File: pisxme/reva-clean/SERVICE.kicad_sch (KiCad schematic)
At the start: 5 parts

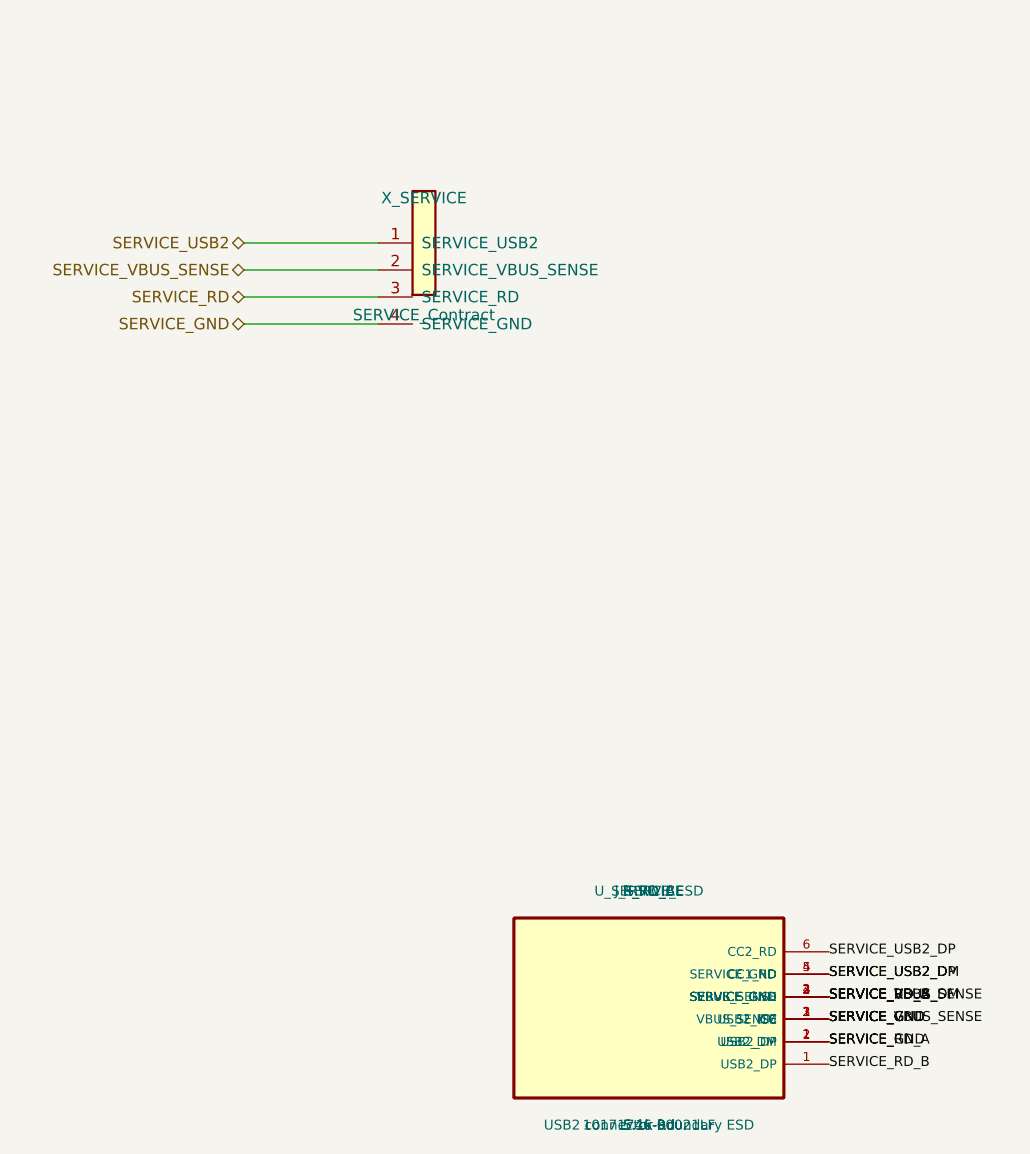
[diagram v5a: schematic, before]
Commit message: fix KiCad annotation and netlist export
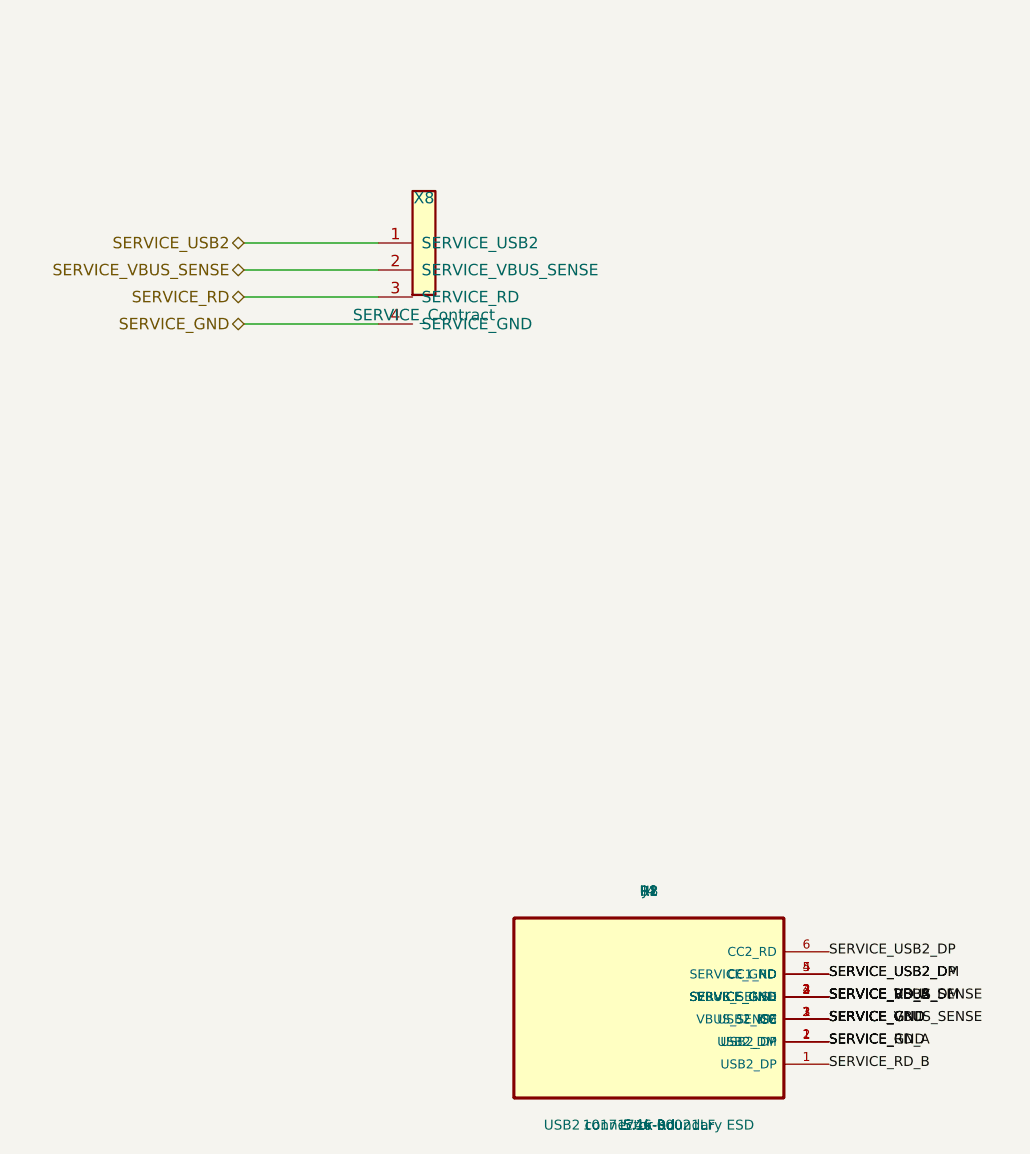
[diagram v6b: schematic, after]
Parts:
- R1: renamed from R_RD_A; footprint (none) -> PiSXMeRevAClean:USB_C_SERVICE_10171746
- U8: renamed from U_SERVICE_ESD; footprint PiSXMeRevAClean:USB_C_SERVICE_10171746 -> (none)
- renumbered J_SERVICE to J4, R_RD_B to R2, X_SERVICE to X8
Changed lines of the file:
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@@
     (on_board no)
     (dnp no)
-    (property "Reference" "X_SERVICE"
+    (property "Reference" "X8"
       (at 25 5 0)
       (effects (font (size 1.27 1.27))))
@@
     (pin "4")
     (instances (project "PiSXMe_RevA_Clean"
-      (path "/30000000-0000-0000-0000-000000000000/10000000-0000-0000-0000-000000000008" (reference "X_SERVICE" ) (unit 1))))
+      (path "/30000000-0000-0000-0000-000000000000/10000000-0000-0000-0000-000000000008" (reference "X8" ) (unit 1))))
   )
 (label "SERVICE_USB2_DP" (at 70 88.75 0) (effects (font (size 1.1 1.1)) (justify left)))
@@
 (label "SERVICE_RD_A" (at 70 98.75 0) (effects (font (size 1.1 1.1)) (justify left)))
 (label "SERVICE_RD_B" (at 70 101.25 0) (effects (font (size 1.1 1.1)) (justify left)))
-(symbol (lib_id "PiSXMeRevAClean:USB2_UFP_CONNECTOR") (at 50 95 0) (unit 1) (exclude_from_sim no) (in_bom yes) (on_board yes) (dnp no) (property "Reference" "J_SERVICE" (at 50 82 0) (effects (font (size 1.1 1.1)))) (property "Value" "10171746-00021LF" (at 50 108 0) (effects (font (size 1.1 1.1)))) (property "MPN" "10171746-00021LF" (at 50 95 0) (effects (font (size 1 1)) (hide yes))) (property "Footprint" "PiSXMeRevAClean:USB_C_SERVICE_10171746" (at 50 95 0) (effects (font (size 1 1)) (hide yes))) (pin "1")
+(symbol (lib_id "PiSXMeRevAClean:USB2_UFP_CONNECTOR") (at 50 95 0) (unit 1) (exclude_from_sim no) (in_bom yes) (on_board yes) (dnp no) (property "Reference" "J4" (at 50 82 0) (effects (font (size 1.1 1.1)))) (property "Value" "10171746-00021LF" (at 50 108 0) (effects (font (size 1.1 1.1)))) (property "MPN" "10171746-00021LF" (at 50 95 0) (effects (font (size 1 1)) (hide yes))) (property "Footprint" "PiSXMeRevAClean:USB_C_SERVICE_10171746" (at 50 95 0) (effects (font (size 1 1)) (hide yes))) (pin "1")
 (pin "2")
 (pin "3")
 (pin "4")
 (pin "5")
-(pin "6") (instances (project "PiSXMe_RevA_Clean" (path "/30000000-0000-0000-0000-000000000000" (reference "J_SERVICE") (unit 1)))) )(label "SERVICE_USB2_DP" (at 70 91.25 0) (effects (font (size 1.1 1.1)) (justify left)))
+(pin "6") (instances (project "PiSXMe_RevA_Clean" (path "/30000000-0000-0000-0000-000000000000" (reference "J4") (unit 1)))) )(label "SERVICE_USB2_DP" (at 70 91.25 0) (effects (font (size 1.1 1.1)) (justify left)))
 (label "SERVICE_USB2_DM" (at 70 93.75 0) (effects (font (size 1.1 1.1)) (justify left)))
 (label "SERVICE_VBUS_SENSE" (at 70 96.25 0) (effects (font (size 1.1 1.1)) (justify left)))
 (label "SERVICE_GND" (at 70 98.75 0) (effects (font (size 1.1 1.1)) (justify left)))
-(symbol (lib_id "PiSXMeRevAClean:USB2_ESD") (at 50 95 0) (unit 1) (exclude_from_sim no) (in_bom yes) (on_board yes) (dnp no) (property "Reference" "U_SERVICE_ESD" (at 50 82 0) (effects (font (size 1.1 1.1)))) (property "Value" "USB2 connector-boundary ESD" (at 50 108 0) (effects (font (size 1.1 1.1)))) (property "MPN" "USB2 connector-boundary ESD" (at 50 95 0) (effects (font (size 1 1)) (hide yes))) (property "Footprint" "PiSXMeRevAClean:USB_C_SERVICE_10171746" (at 50 95 0) (effects (font (size 1 1)) (hide yes))) (pin "1")
+(symbol (lib_id "PiSXMeRevAClean:USB2_ESD") (at 50 95 0) (unit 1) (exclude_from_sim no) (in_bom yes) (on_board yes) (dnp no) (property "Reference" "U8" (at 50 82 0) (effects (font (size 1.1 1.1)))) (property "Value" "USB2 connector-boundary ESD" (at 50 108 0) (effects (font (size 1.1 1.1)))) (property "MPN" "USB2 connector-boundary ESD" (at 50 95 0) (effects (font (size 1 1)) (hide yes))) (property "Footprint" "" (at 50 95 0) (effects (font (size 1 1)) (hide yes))) (pin "1")
 (pin "2")
 (pin "3")
-(pin "4") (instances (project "PiSXMe_RevA_Clean" (path "/30000000-0000-0000-0000-000000000000" (reference "U_SERVICE_ESD") (unit 1)))) )(label "SERVICE_RD_A" (at 70 93.75 0) (effects (font (size 1.1 1.1)) (justify left)))
+(pin "4") (instances (project "PiSXMe_RevA_Clean" (path "/30000000-0000-0000-0000-000000000000" (reference "U8") (unit 1)))) )(label "SERVICE_RD_A" (at 70 93.75 0) (effects (font (size 1.1 1.1)) (justify left)))
 (label "SERVICE_GND" (at 70 96.25 0) (effects (font (size 1.1 1.1)) (justify left)))
-(symbol (lib_id "PiSXMeRevAClean:USB2_RD_5K1") (at 50 95 0) (unit 1) (exclude_from_sim no) (in_bom yes) (on_board yes) (dnp no) (property "Reference" "R_RD_A" (at 50 82 0) (effects (font (size 1.1 1.1)))) (property "Value" "5.1k Rd" (at 50 108 0) (effects (font (size 1.1 1.1)))) (property "MPN" "5.1k Rd" (at 50 95 0) (effects (font (size 1 1)) (hide yes))) (property "Footprint" "" (at 50 95 0) (effects (font (size 1 1)) (hide yes))) (pin "1")
-(pin "2") (instances (project "PiSXMe_RevA_Clean" (path "/30000000-0000-0000-0000-000000000000" (reference "R_RD_A") (unit 1)))) )(label "SERVICE_RD_B" (at 70 93.75 0) (effects (font (size 1.1 1.1)) (justify left)))
+(symbol (lib_id "PiSXMeRevAClean:USB2_RD_5K1") (at 50 95 0) (unit 1) (exclude_from_sim no) (in_bom yes) (on_board yes) (dnp no) (property "Reference" "R1" (at 50 82 0) (effects (font (size 1.1 1.1)))) (property "Value" "5.1k Rd" (at 50 108 0) (effects (font (size 1.1 1.1)))) (property "MPN" "5.1k Rd" (at 50 95 0) (effects (font (size 1 1)) (hide yes))) (property "Footprint" "PiSXMeRevAClean:USB_C_SERVICE_10171746" (at 50 95 0) (effects (font (size 1 1)) (hide yes))) (pin "1")
+(pin "2") (instances (project "PiSXMe_RevA_Clean" (path "/30000000-0000-0000-0000-000000000000" (reference "R1") (unit 1)))) )(label "SERVICE_RD_B" (at 70 93.75 0) (effects (font (size 1.1 1.1)) (justify left)))
 (label "SERVICE_GND" (at 70 96.25 0) (effects (font (size 1.1 1.1)) (justify left)))
-(symbol (lib_id "PiSXMeRevAClean:USB2_RD_5K1") (at 50 95 0) (unit 1) (exclude_from_sim no) (in_bom yes) (on_board yes) (dnp no) (property "Reference" "R_RD_B" (at 50 82 0) (effects (font (size 1.1 1.1)))) (property "Value" "5.1k Rd" (at 50 108 0) (effects (font (size 1.1 1.1)))) (property "MPN" "5.1k Rd" (at 50 95 0) (effects (font (size 1 1)) (hide yes))) (property "Footprint" "" (at 50 95 0) (effects (font (size 1 1)) (hide yes))) (pin "1")
-(pin "2") (instances (project "PiSXMe_RevA_Clean" (path "/30000000-0000-0000-0000-000000000000" (reference "R_RD_B") (unit 1)))) )
+(symbol (lib_id "PiSXMeRevAClean:USB2_RD_5K1") (at 50 95 0) (unit 1) (exclude_from_sim no) (in_bom yes) (on_board yes) (dnp no) (property "Reference" "R2" (at 50 82 0) (effects (font (size 1.1 1.1)))) (property "Value" "5.1k Rd" (at 50 108 0) (effects (font (size 1.1 1.1)))) (property "MPN" "5.1k Rd" (at 50 95 0) (effects (font (size 1 1)) (hide yes))) (property "Footprint" "" (at 50 95 0) (effects (font (size 1 1)) (hide yes))) (pin "1")
+(pin "2") (instances (project "PiSXMe_RevA_Clean" (path "/30000000-0000-0000-0000-000000000000" (reference "R2") (unit 1)))) )
   (sheet_instances (path "/30000000-0000-0000-0000-000000000000/10000000-0000-0000-0000-000000000008" (page "8")))
 )

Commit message: close service ESD electrical authority
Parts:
- U8: value USB2 connector-boundary ESD -> TPD2EUSB30DRTR; footprint (none) -> PiSXMeRevAClean:USB_C_SERVICE_10171746; MPN USB2 connector-boundary ESD -> TPD2EUSB30DRTR
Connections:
- net SERVICE_GND: no longer U8.4 (SERVICE_GND)
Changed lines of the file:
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@@
 (label "SERVICE_VBUS_SENSE" (at 70 96.25 0) (effects (font (size 1.1 1.1)) (justify left)))
 (label "SERVICE_GND" (at 70 98.75 0) (effects (font (size 1.1 1.1)) (justify left)))
-(symbol (lib_id "PiSXMeRevAClean:USB2_ESD") (at 50 95 0) (unit 1) (exclude_from_sim no) (in_bom yes) (on_board yes) (dnp no) (property "Reference" "U8" (at 50 82 0) (effects (font (size 1.1 1.1)))) (property "Value" "USB2 connector-boundary ESD" (at 50 108 0) (effects (font (size 1.1 1.1)))) (property "MPN" "USB2 connector-boundary ESD" (at 50 95 0) (effects (font (size 1 1)) (hide yes))) (property "Footprint" "" (at 50 95 0) (effects (font (size 1 1)) (hide yes))) (pin "1")
+(label "SERVICE_USB2_DP" (at 70 92.5 0) (effects (font (size 1.1 1.1)) (justify left)))
+(label "SERVICE_USB2_DM" (at 70 95 0) (effects (font (size 1.1 1.1)) (justify left)))
+(label "SERVICE_GND" (at 70 97.5 0) (effects (font (size 1.1 1.1)) (justify left)))
+(symbol (lib_id "PiSXMeRevAClean:USB2_ESD") (at 50 95 0) (unit 1) (exclude_from_sim no) (in_bom yes) (on_board yes) (dnp no) (property "Reference" "U8" (at 50 82 0) (effects (font (size 1.1 1.1)))) (property "Value" "TPD2EUSB30DRTR" (at 50 108 0) (effects (font (size 1.1 1.1)))) (property "MPN" "TPD2EUSB30DRTR" (at 50 95 0) (effects (font (size 1 1)) (hide yes))) (property "Footprint" "PiSXMeRevAClean:USB_C_SERVICE_10171746" (at 50 95 0) (effects (font (size 1 1)) (hide yes))) (pin "1")
 (pin "2")
-(pin "3")
-(pin "4") (instances (project "PiSXMe_RevA_Clean" (path "/30000000-0000-0000-0000-000000000000" (reference "U8") (unit 1)))) )(label "SERVICE_RD_A" (at 70 93.75 0) (effects (font (size 1.1 1.1)) (justify left)))
+(pin "3") (instances (project "PiSXMe_RevA_Clean" (path "/30000000-0000-0000-0000-000000000000" (reference "U8") (unit 1)))) )(label "SERVICE_RD_A" (at 70 93.75 0) (effects (font (size 1.1 1.1)) (justify left)))
 (label "SERVICE_GND" (at 70 96.25 0) (effects (font (size 1.1 1.1)) (justify left)))
 (symbol (lib_id "PiSXMeRevAClean:USB2_RD_5K1") (at 50 95 0) (unit 1) (exclude_from_sim no) (in_bom yes) (on_board yes) (dnp no) (property "Reference" "R1" (at 50 82 0) (effects (font (size 1.1 1.1)))) (property "Value" "5.1k Rd" (at 50 108 0) (effects (font (size 1.1 1.1)))) (property "MPN" "5.1k Rd" (at 50 95 0) (effects (font (size 1 1)) (hide yes))) (property "Footprint" "PiSXMeRevAClean:USB_C_SERVICE_10171746" (at 50 95 0) (effects (font (size 1 1)) (hide yes))) (pin "1")

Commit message: close service ESD footprint authority
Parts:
- R1: footprint PiSXMeRevAClean:USB_C_SERVICE_10171746 -> PiSXMeRevAClean:R_0402_1005Metric
- R2: footprint (none) -> PiSXMeRevAClean:R_0402_1005Metric
- U8: footprint PiSXMeRevAClean:USB_C_SERVICE_10171746 -> PiSXMeRevAClean:Texas_DRT_3
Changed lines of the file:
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@@
 (label "SERVICE_USB2_DM" (at 70 95 0) (effects (font (size 1.1 1.1)) (justify left)))
 (label "SERVICE_GND" (at 70 97.5 0) (effects (font (size 1.1 1.1)) (justify left)))
-(symbol (lib_id "PiSXMeRevAClean:USB2_ESD") (at 50 95 0) (unit 1) (exclude_from_sim no) (in_bom yes) (on_board yes) (dnp no) (property "Reference" "U8" (at 50 82 0) (effects (font (size 1.1 1.1)))) (property "Value" "TPD2EUSB30DRTR" (at 50 108 0) (effects (font (size 1.1 1.1)))) (property "MPN" "TPD2EUSB30DRTR" (at 50 95 0) (effects (font (size 1 1)) (hide yes))) (property "Footprint" "PiSXMeRevAClean:USB_C_SERVICE_10171746" (at 50 95 0) (effects (font (size 1 1)) (hide yes))) (pin "1")
+(symbol (lib_id "PiSXMeRevAClean:USB2_ESD") (at 50 95 0) (unit 1) (exclude_from_sim no) (in_bom yes) (on_board yes) (dnp no) (property "Reference" "U8" (at 50 82 0) (effects (font (size 1.1 1.1)))) (property "Value" "TPD2EUSB30DRTR" (at 50 108 0) (effects (font (size 1.1 1.1)))) (property "MPN" "TPD2EUSB30DRTR" (at 50 95 0) (effects (font (size 1 1)) (hide yes))) (property "Footprint" "PiSXMeRevAClean:Texas_DRT_3" (at 50 95 0) (effects (font (size 1 1)) (hide yes))) (pin "1")
 (pin "2")
 (pin "3") (instances (project "PiSXMe_RevA_Clean" (path "/30000000-0000-0000-0000-000000000000" (reference "U8") (unit 1)))) )(label "SERVICE_RD_A" (at 70 93.75 0) (effects (font (size 1.1 1.1)) (justify left)))
 (label "SERVICE_GND" (at 70 96.25 0) (effects (font (size 1.1 1.1)) (justify left)))
-(symbol (lib_id "PiSXMeRevAClean:USB2_RD_5K1") (at 50 95 0) (unit 1) (exclude_from_sim no) (in_bom yes) (on_board yes) (dnp no) (property "Reference" "R1" (at 50 82 0) (effects (font (size 1.1 1.1)))) (property "Value" "5.1k Rd" (at 50 108 0) (effects (font (size 1.1 1.1)))) (property "MPN" "5.1k Rd" (at 50 95 0) (effects (font (size 1 1)) (hide yes))) (property "Footprint" "PiSXMeRevAClean:USB_C_SERVICE_10171746" (at 50 95 0) (effects (font (size 1 1)) (hide yes))) (pin "1")
+(symbol (lib_id "PiSXMeRevAClean:USB2_RD_5K1") (at 50 95 0) (unit 1) (exclude_from_sim no) (in_bom yes) (on_board yes) (dnp no) (property "Reference" "R1" (at 50 82 0) (effects (font (size 1.1 1.1)))) (property "Value" "5.1k Rd" (at 50 108 0) (effects (font (size 1.1 1.1)))) (property "MPN" "5.1k Rd" (at 50 95 0) (effects (font (size 1 1)) (hide yes))) (property "Footprint" "PiSXMeRevAClean:R_0402_1005Metric" (at 50 95 0) (effects (font (size 1 1)) (hide yes))) (pin "1")
 (pin "2") (instances (project "PiSXMe_RevA_Clean" (path "/30000000-0000-0000-0000-000000000000" (reference "R1") (unit 1)))) )(label "SERVICE_RD_B" (at 70 93.75 0) (effects (font (size 1.1 1.1)) (justify left)))
 (label "SERVICE_GND" (at 70 96.25 0) (effects (font (size 1.1 1.1)) (justify left)))
-(symbol (lib_id "PiSXMeRevAClean:USB2_RD_5K1") (at 50 95 0) (unit 1) (exclude_from_sim no) (in_bom yes) (on_board yes) (dnp no) (property "Reference" "R2" (at 50 82 0) (effects (font (size 1.1 1.1)))) (property "Value" "5.1k Rd" (at 50 108 0) (effects (font (size 1.1 1.1)))) (property "MPN" "5.1k Rd" (at 50 95 0) (effects (font (size 1 1)) (hide yes))) (property "Footprint" "" (at 50 95 0) (effects (font (size 1 1)) (hide yes))) (pin "1")
+(symbol (lib_id "PiSXMeRevAClean:USB2_RD_5K1") (at 50 95 0) (unit 1) (exclude_from_sim no) (in_bom yes) (on_board yes) (dnp no) (property "Reference" "R2" (at 50 82 0) (effects (font (size 1.1 1.1)))) (property "Value" "5.1k Rd" (at 50 108 0) (effects (font (size 1.1 1.1)))) (property "MPN" "5.1k Rd" (at 50 95 0) (effects (font (size 1 1)) (hide yes))) (property "Footprint" "PiSXMeRevAClean:R_0402_1005Metric" (at 50 95 0) (effects (font (size 1 1)) (hide yes))) (pin "1")
 (pin "2") (instances (project "PiSXMe_RevA_Clean" (path "/30000000-0000-0000-0000-000000000000" (reference "R2") (unit 1)))) )
   (sheet_instances (path "/30000000-0000-0000-0000-000000000000/10000000-0000-0000-0000-000000000008" (page "8")))
